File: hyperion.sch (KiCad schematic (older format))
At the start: 45 parts

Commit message: Updated
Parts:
- removed CON?: USB-MINI-B, symbol USB-MINI-B
- removed U?: 4017, symbol 4017
- added CON1: USB-MINI-B-CONN, symbol USB-MINI-B-CONN
- added R10, R11, R12, R13, R14, R15, R6, R7, R8, R9: 50, ~, symbol R
- added U3: CD4017, symbol CD4017
- R4: renamed from R?; value 282 -> 658
- gave numbers to parts that had none: 42
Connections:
- net labels added: LED_CLK
- wire segments 126 -> 146
- no-connect marks 9 -> 11
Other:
- note added: "Output should be 3V.\n3 = 1.25(1 + 470/658)"
- moved on the sheet: C1, C10, C2, C3, C4, C5, C6, C7, C8, C9, D1, D10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

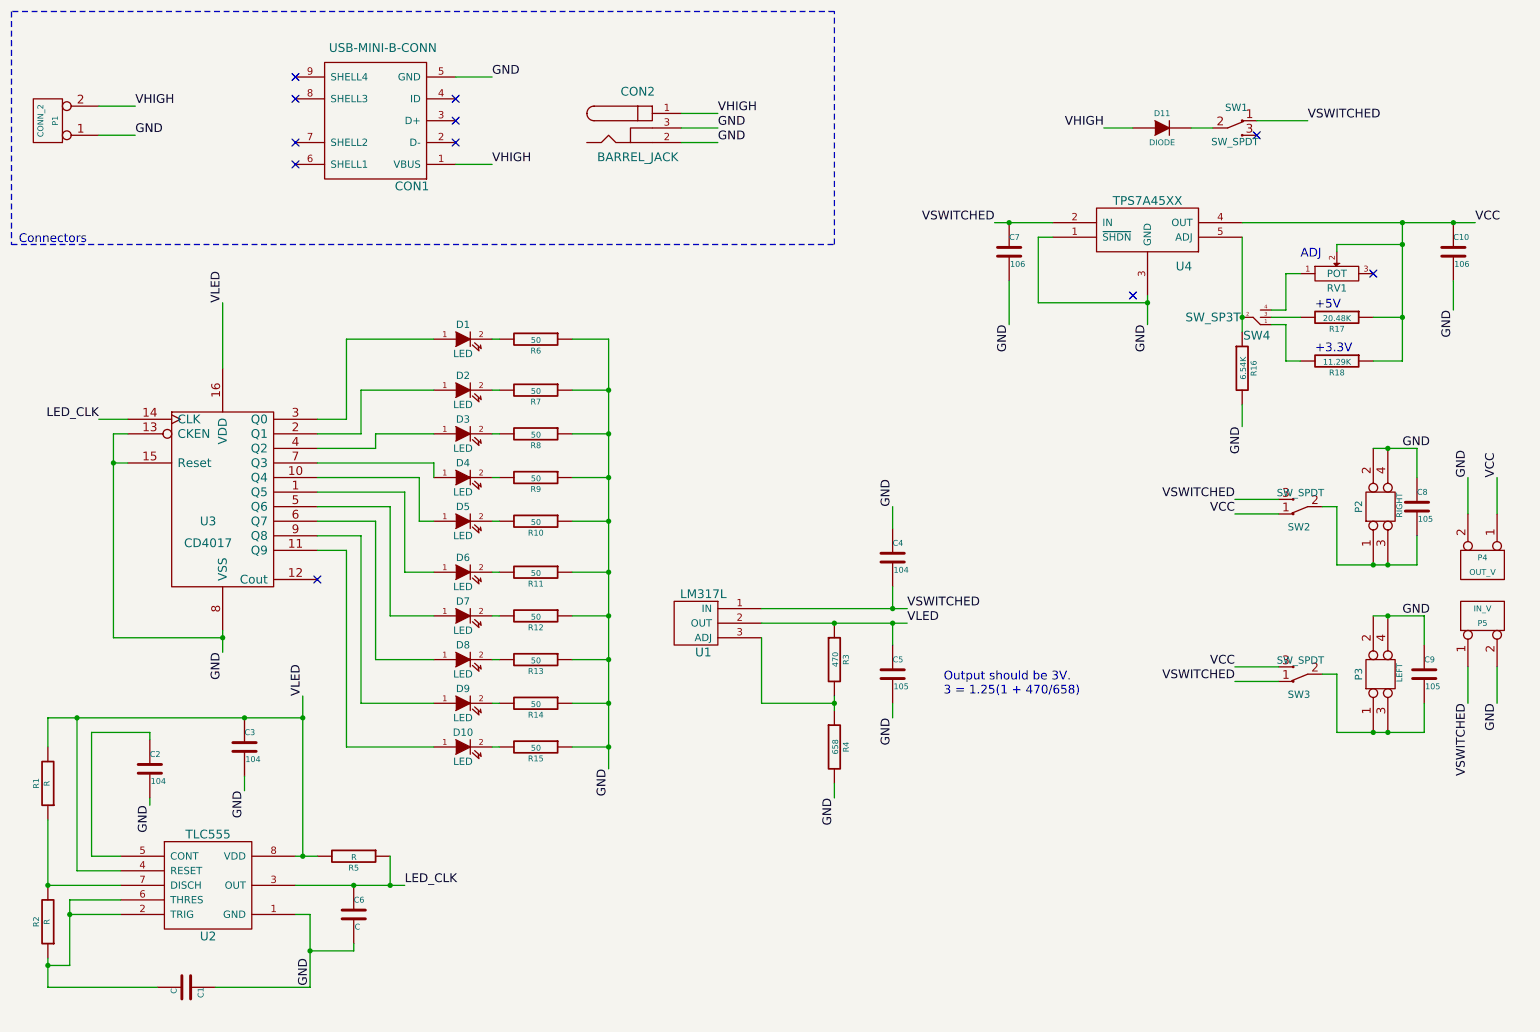
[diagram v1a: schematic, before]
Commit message: Beginning PCB.
Need to get dimensions of breadboard
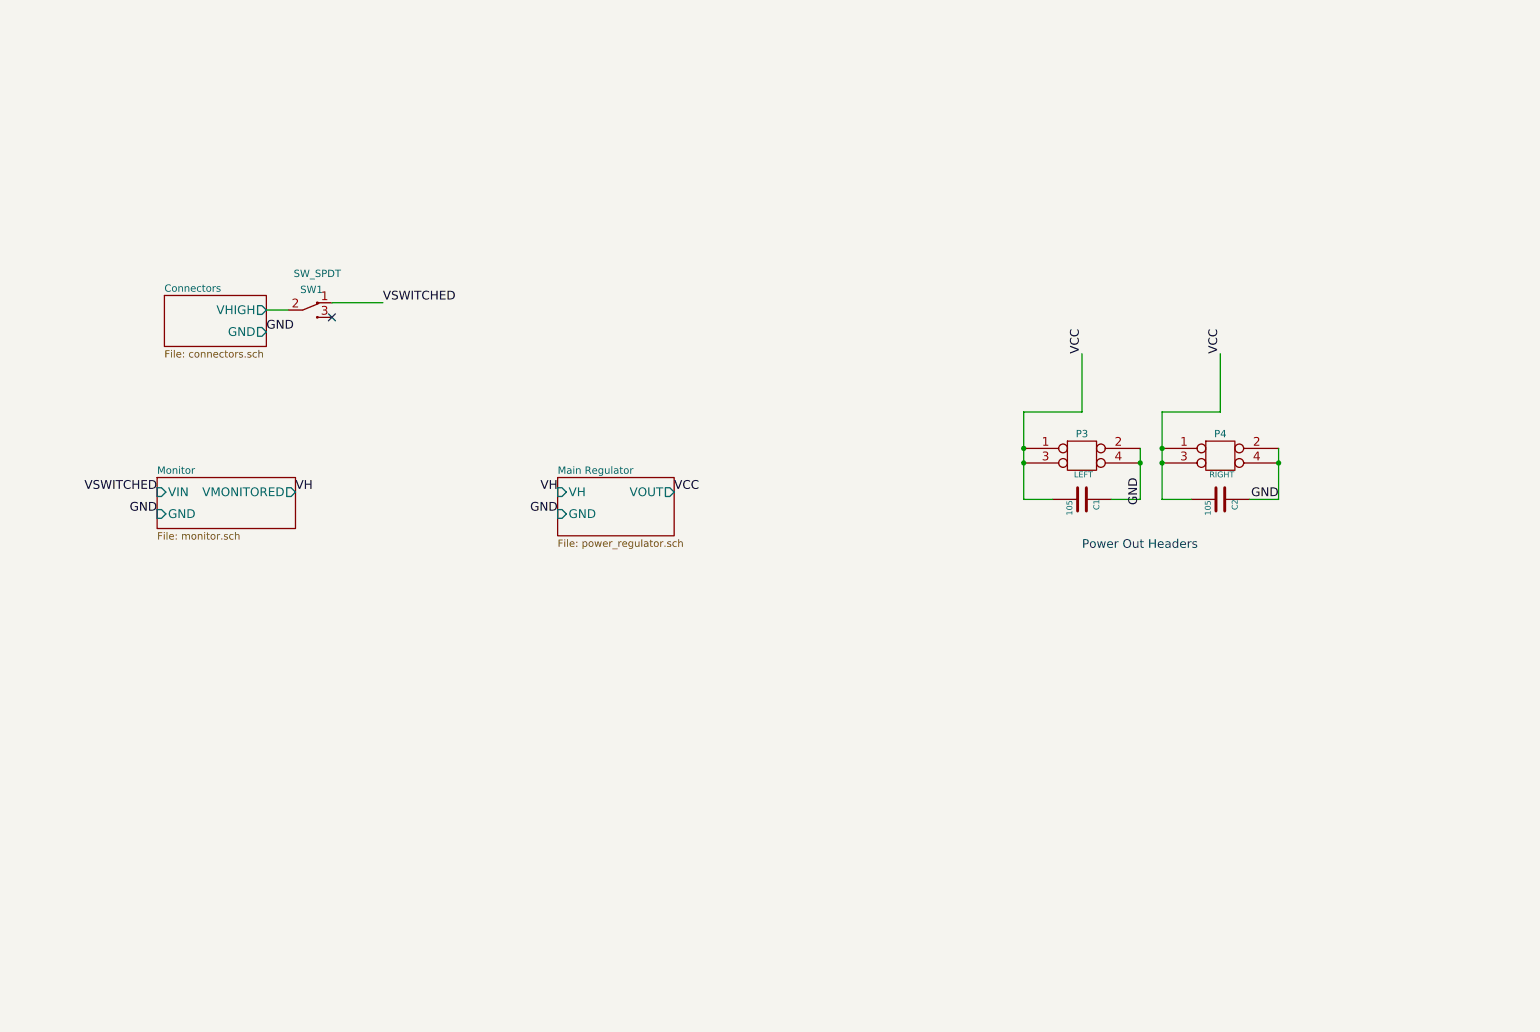
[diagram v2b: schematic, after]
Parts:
- removed C1, C6: C, ~, symbol C
- removed C10, C7: 106, ~, symbol C
- removed C2, C3, C4: 104, ~, symbol C
- removed C5: 105, ~, symbol C
- removed CON1: USB-MINI-B-CONN, symbol USB-MINI-B-CONN
- removed CON2: BARREL_JACK, symbol BARREL_JACK
- removed D1, D10, D2, D3, D4, D5, D6, D7, D8, D9: LED, ~, symbol LED
- removed D11: DIODE, ~, symbol DIODE
- removed P1: CONN_2, symbol CONN_2
- removed P4: OUT_V, symbol CONN_2
- removed P5: IN_V, symbol CONN_2
- removed R1, R2, R5: R, ~, symbol R
- removed R10, R11, R12, R13, R14, R15, R6, R7, R8, R9: 50, ~, symbol R
- removed R16: 6.54K, ~, symbol R
- removed R17: 20.48K, ~, symbol R
- removed R18: 11.29K, ~, symbol R
- removed R3: 470, ~, symbol R
- removed R4: 658, ~, symbol R
- removed RV1: POT, ~, symbol POT
- removed SW2, SW3: SW_SPDT, symbol SW_SPDT
- removed SW4: SW_SP3T, symbol SW_SP3T
- removed U1: LM317L, symbol LM317L
- removed U2: TLC555, symbol TLC555
- removed U3: CD4017, symbol CD4017
- removed U4: TPS7A45XX, ~, symbol TPS7A45XX
- renumbered C9 to C1, C8 to C2, P2 to P4
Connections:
- net VCC: now also C1.2, C2.2, P3.1, P3.3, P4.1, P4.3
- net Connectors/VHIGH: now reaches SW1.2 (COM)
- no-connect marks 11 -> 1
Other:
- note added: "Power Out Headers"
- note removed: "+3.3V"
- note removed: "+5V\n"
- note removed: "ADJ"
- note removed: "Connectors"
- note removed: "Output should be 3V.\n3 = 1.25(1 + 470/658)"
- moved on the sheet: C1, C2, P3, P4, SW1
